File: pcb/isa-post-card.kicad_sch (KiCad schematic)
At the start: 31 parts, among them J2 POWER, J3 Bus_ISA_8bit_AB_Rev0, J4 Atmel-JTAG-10, SW1 SW_DIP_x05, SW2 SW_DIP_x05, U1 74HCT688, U2 74HCT688, U3 ATF1504AS-xJx44, U5 D168K, U6 D168K

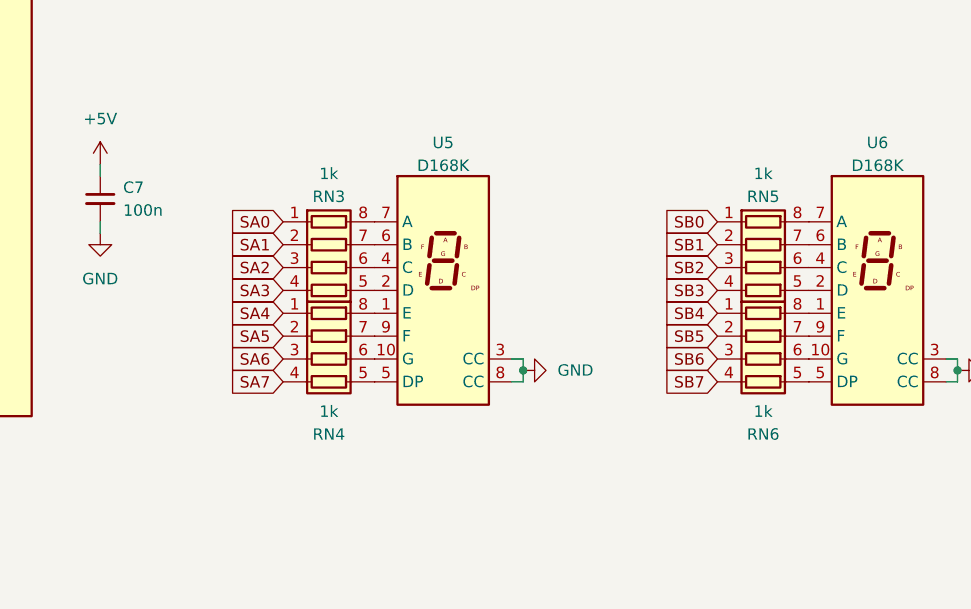
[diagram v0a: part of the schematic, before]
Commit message: Fixing design bugs and adding CUPL code
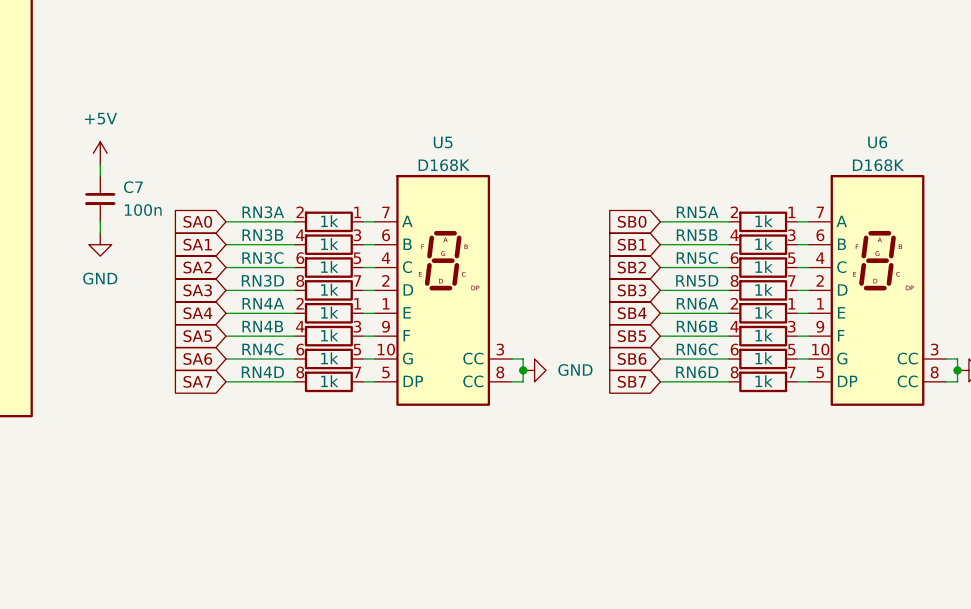
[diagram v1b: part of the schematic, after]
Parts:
- removed RN3, RN4, RN5, RN6: 1k, Resistor_THT:R_Array_SIP8, symbol Device:R_Pack04
- added RN3, RN4, RN5, RN6: 1k, Resistor_THT:R_Array_SIP8, symbol Device:R_Pack04_SIP_Split
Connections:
- net SA0: now also RN3.2 (R1.2)
- net SA1: now also RN3.4 (R2.2)
- net SA2: now also RN3.6 (R3.2)
- net SA3: now also RN3.8 (R4.2)
- net SA4: now also RN4.2 (R1.2)
- net SA5: now also RN4.4 (R2.2)
- net SA6: now also RN4.6 (R3.2)
- net SA7: now also RN4.8 (R4.2)
- net SB0: now also RN5.2 (R1.2)
- net SB1: now also RN5.4 (R2.2)
- net SB2: now also RN5.6 (R3.2)
- net SB3: now also RN5.8 (R4.2)
- net SB4: now also RN6.2 (R1.2)
- net SB5: now also RN6.4 (R2.2)
- net SB6: now also RN6.6 (R3.2)
- net SB7: now also RN6.8 (R4.2)
- net at U6.2 (D): now also RN5.7 (R4.1)
- net at U6.4 (C): now also RN5.5 (R3.1)
- net at U6.6 (B): now also RN5.3 (R2.1)
- net at U6.7 (A): now also RN5.1 (R1.1)
- net at U5.5 (DP): now also RN4.7 (R4.1)
- net at U5.10 (G): now also RN4.5 (R3.1)
- net at U5.9 (F): now also RN4.3 (R2.1)
- net at U5.1 (E): now also RN4.1 (R1.1)
- net at U5.2 (D): now also RN3.7 (R4.1)
- net at U5.4 (C): now also RN3.5 (R3.1)
- net at U5.6 (B): now also RN3.3 (R2.1)
- net at U5.7 (A): now also RN3.1 (R1.1)
- net at U6.1 (E): now also RN6.1 (R1.1)
- net at U6.10 (G): now also RN6.5 (R3.1)
- net at U6.5 (DP): now also RN6.7 (R4.1)
- net at U6.9 (F): now also RN6.3 (R2.1)

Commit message: Revising schematics
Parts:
- added C8: 100n, Capacitor_THT:C_Disc_D5.0mm_W2.5mm_P5.00mm, symbol Device:C_Small
- added D5: CLK, LED_THT:LED_D5.0mm, symbol Device:LED
- added D6: RESET, LED_THT:LED_D5.0mm, symbol Device:LED
- added R5: 1k, Resistor_THT:R_Axial_DIN0207_L6.3mm_D2.5mm_P7.62mm_Horizontal, symbol Device:R
- added R6: 500, Resistor_THT:R_Axial_DIN0207_L6.3mm_D2.5mm_P7.62mm_Horizontal, symbol Device:R
- added U4: 74HC00, Package_DIP:DIP-14_W7.62mm_Socket, symbol 74xx:74HC00
- J4: value Atmel-JTAG-10 -> PROGRAMMER
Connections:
- net +5V: now also C8.1, U4.14 (VCC)
- net D0: now also U3.20 (I/O); no longer U3.29 (I/O)
- net D1: now also U3.21 (I/O); no longer U3.31 (I/O)
- net D2: now also U3.24 (I/O); no longer U3.33 (I/O)
- net D3: now also U3.25 (I/O/PD2); no longer U3.34 (I/O)
- net D4: now also U3.26 (I/O); no longer U3.36 (I/O)
- net D5: now also U3.27 (I/O); no longer U3.37 (I/O)
- net D6: now also U3.28 (I/O); no longer U3.39 (I/O)
- net D7: now also U3.29 (I/O); no longer U3.40 (I/O)
- net GND: now also C8.2, D5.1 (K), D6.1 (K), U4.7 (GND)
- net RES: now also U4.10, U4.9
- net SA0: now also RN4.6 (R3.2), U3.14 (I/O); no longer RN3.2 (R1.2), U3.4 (I/O)
- net SA1: now also RN4.8 (R4.2), U3.12 (I/O); no longer RN3.4 (R2.2), U3.5 (I/O)
- net SA2: now also U3.11 (I/O/PD1); no longer U3.6 (I/O)
- net SA3: now also RN3.4 (R2.2), U3.16 (I/O); no longer RN3.8 (R4.2), U3.8 (I/O)
- net SA4: now also RN3.2 (R1.2), U3.19 (I/O); no longer RN4.2 (R1.2), U3.9 (I/O)
- net SA5: now also U3.17 (I/O); no longer U3.12 (I/O)
- net SA6: now also RN4.2 (R1.2), U3.18 (I/O); no longer RN4.6 (R3.2), U3.14 (I/O)
- net SA7: now also RN3.8 (R4.2), U3.9 (I/O); no longer RN4.8 (R4.2), U3.16 (I/O)
- net SB0: now also RN5.8 (R4.2), U3.37 (I/O); no longer RN5.2 (R1.2), U3.17 (I/O)
- net SB1: now also RN5.6 (R3.2), U3.40 (I/O); no longer RN5.4 (R2.2), U3.18 (I/O)
- net SB2: now also RN5.2 (R1.2), U3.6 (I/O); no longer RN5.6 (R3.2), U3.19 (I/O)
- net SB3: now also RN6.4 (R2.2), U3.5 (I/O); no longer RN5.8 (R4.2), U3.20 (I/O)
- net SB4: now also U3.4 (I/O); no longer U3.21 (I/O)
- net SB5: now also RN6.6 (R3.2), U3.41 (I/O/GCLK3); no longer RN6.4 (R2.2), U3.24 (I/O)
- net SB6: now also RN6.8 (R4.2), U3.39 (I/O); no longer RN6.6 (R3.2), U3.26 (I/O)
- net SB7: now also RN5.4 (R2.2), U3.8 (I/O); no longer RN6.8 (R4.2), U3.27 (I/O)
- net ~{SEL1}: now also U3.34 (I/O); no longer U3.28 (I/O)
- net ~{SEL2}: now also U3.31 (I/O); no longer U3.41 (I/O/GCLK3)
- net at RN3.1 (R1.1): now also U5.1 (E); no longer U5.7 (A)
- net at RN4.1 (R1.1): now also U5.10 (G); no longer U5.1 (E)
- net at RN5.7 (R4.1): now also U6.7 (A); no longer U6.2 (D)
- net at RN4.5 (R3.1): now also U5.7 (A); no longer U5.10 (G)
- net at RN3.3 (R2.1): now also U5.2 (D); no longer U5.6 (B)
- net at U6.10 (G): now also RN6.7 (R4.1); no longer RN6.5 (R3.1)
- net at U6.4 (C): now also RN5.1 (R1.1); no longer RN5.5 (R3.1)
- net at U6.5 (DP): now also RN5.3 (R2.1); no longer RN6.7 (R4.1)
- net at U6.6 (B): now also RN5.5 (R3.1); no longer RN5.3 (R2.1)
- net at RN6.3 (R2.1): now also U6.2 (D); no longer U6.9 (F)
- net at RN3.7 (R4.1): now also U5.5 (DP); no longer U5.2 (D)
- net at RN4.7 (R4.1): now also U5.6 (B); no longer U5.5 (DP)
- net CLK: now reaches J3.B20 (CLK)
- net CLK: now also U4.1, U4.2
- new net: D6.2 (A), R5.2
- new net: D5.2 (A), R6.2
- new net: R5.1, U4.11
- new net: U4.3, U4.4, U4.5
- new net: U4.12, U4.13, U4.8
- new net: RN6.5 (R3.1), U6.9 (F)
- new net: R6.1, U4.6
- no-connect marks 43 -> 42
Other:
- moved on the sheet: D1, D2, D3, D4, R1, R2, R3, R4, RN3A, RN3B, RN3D, RN4A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
